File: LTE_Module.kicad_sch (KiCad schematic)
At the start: 57 parts, among them J4 Conn_Coaxial, J8 SIM_Card, Q3 MMBT3904, Q4 BC849, Q5 MMBT3904, Q6 MMBT3904, U10 MIC29302AWD, U6 A7670E, U9 AMS1117-3.3

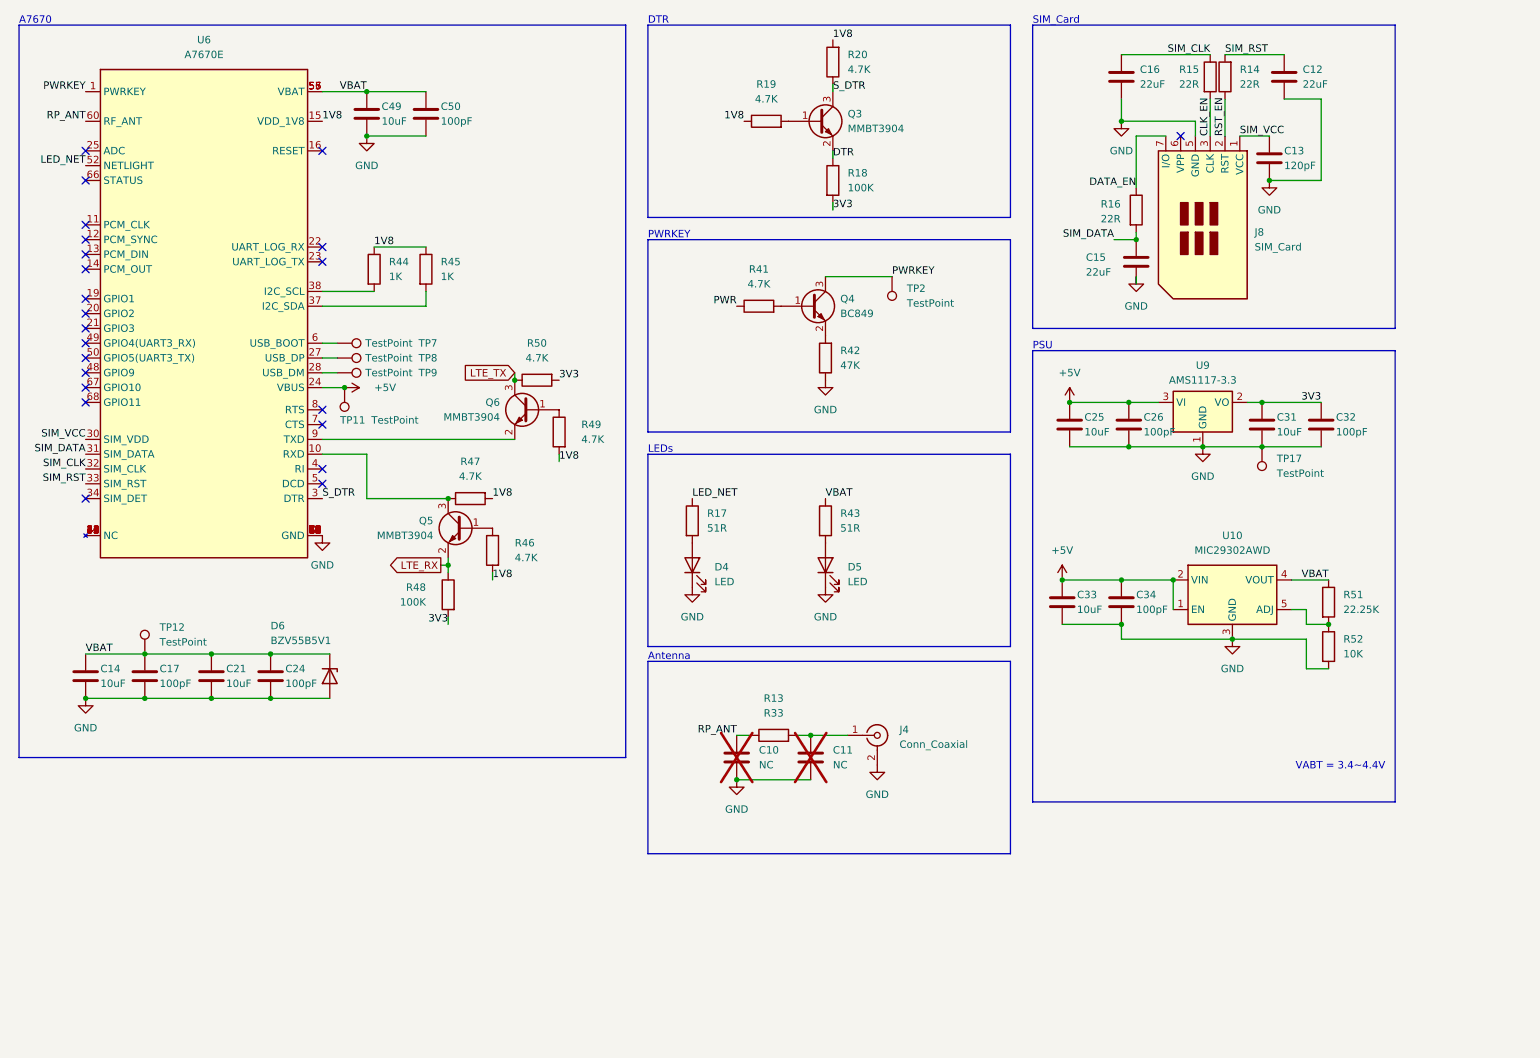
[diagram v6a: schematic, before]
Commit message: assigned most footprints
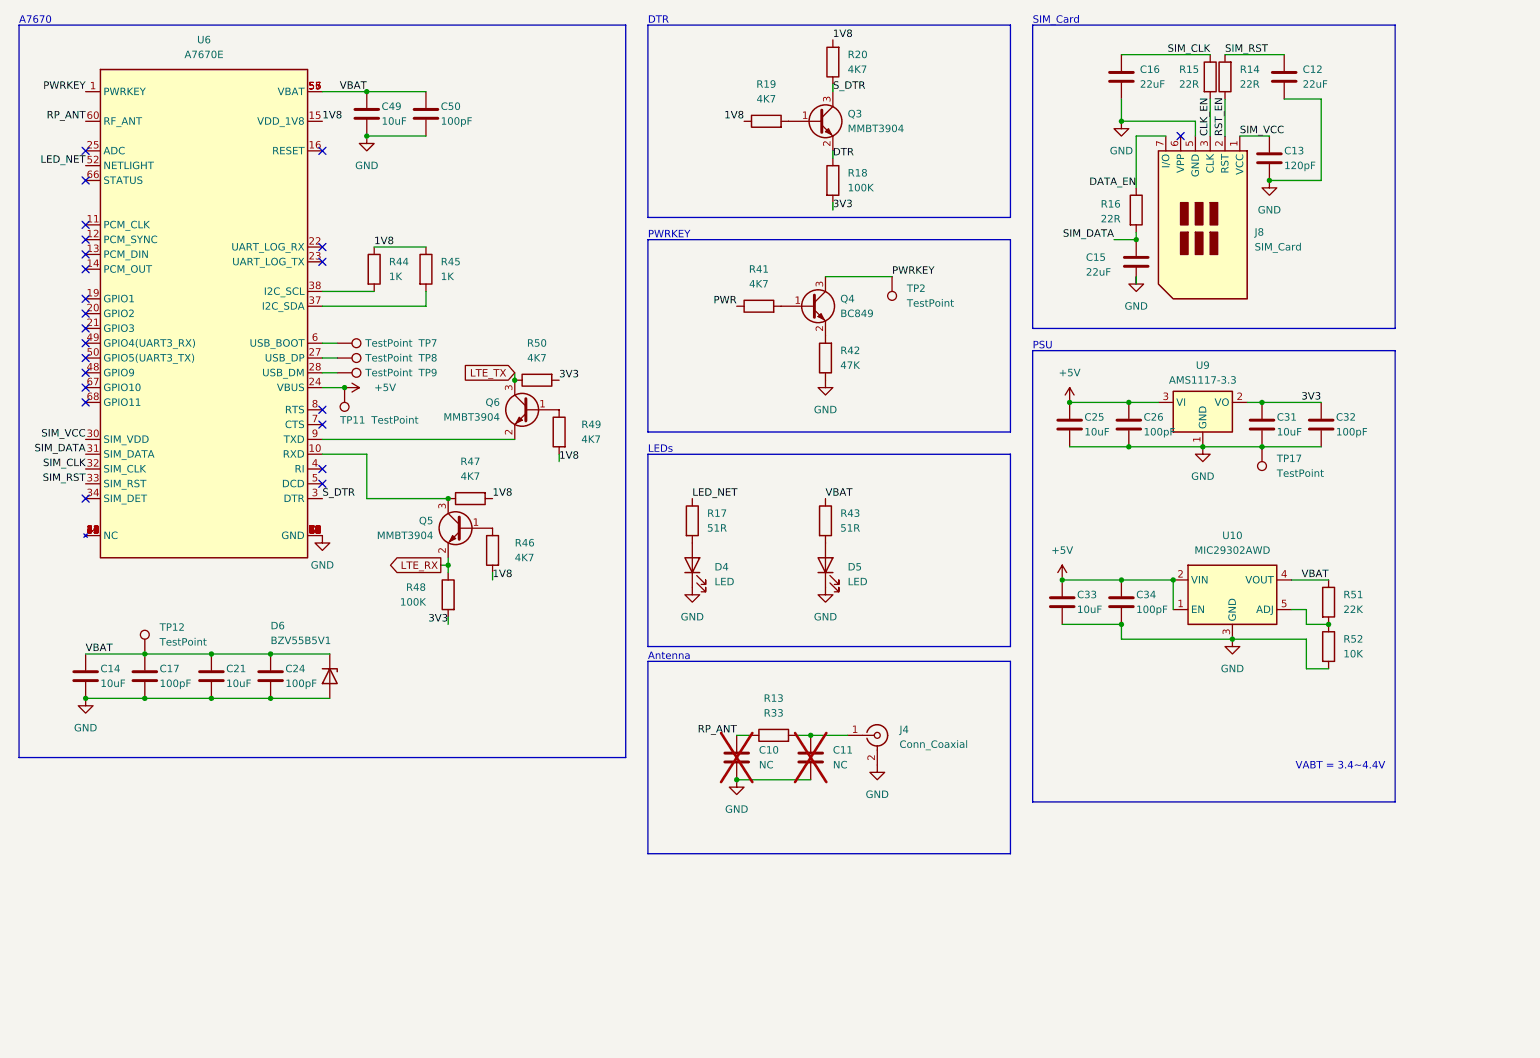
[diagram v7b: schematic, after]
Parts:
- C12, C15, C16: footprint Capacitor_SMD:C_1206_3216Metric_Pad1.33x1.80mm_HandSolder -> (none)
- J8: footprint (none) -> Connector_JAE:JAE_SIM_Card_SF72S006
- R13, R14, R15, R16, R17, R18, R42, R43, R44, R45, R48, R52: footprint (none) -> Resistor_SMD:R_0603_1608Metric
- R19, R20, R41, R46, R47, R49, R50: value 4.7K -> 4K7; footprint (none) -> Resistor_SMD:R_0603_1608Metric
- R51: value 22.25K -> 22K; footprint (none) -> Resistor_SMD:R_0603_1608Metric
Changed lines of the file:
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@@
 			)
 		)
-		(property "Footprint" "Capacitor_SMD:C_1206_3216Metric_Pad1.33x1.80mm_HandSolder"
+		(property "Footprint" ""
 			(at 206.7052 29.21 0)
 			(effects
@@
 			)
 		)
-		(property "Value" "22.25K"
+		(property "Value" "22K"
 			(at 243.84 116.8399 0)
 			(effects
@@
 			)
 		)
-		(property "Footprint" ""
+		(property "Footprint" "Resistor_SMD:R_0603_1608Metric"
 			(at 239.522 115.57 90)
 			(effects
@@
 			)
 		)
-		(property "Value" "4.7K"
+		(property "Value" "4K7"
 			(at 143.51 60.96 90)
 			(effects
@@
 			)
 		)
-		(property "Footprint" ""
+		(property "Footprint" "Resistor_SMD:R_0603_1608Metric"
 			(at 143.51 66.548 90)
 			(effects
@@
 			)
 		)
-		(property "Footprint" "Capacitor_SMD:C_1206_3216Metric_Pad1.33x1.80mm_HandSolder"
+		(property "Footprint" ""
 			(at 234.6452 29.21 0)
 			(effects
@@
 			)
 		)
-		(property "Footprint" ""
+		(property "Footprint" "Resistor_SMD:R_0603_1608Metric"
 			(at 225.298 25.4 90)
 			(effects
@@
 			)
 		)
-		(property "Value" "4.7K"
+		(property "Value" "4K7"
 			(at 101.6 107.9499 0)
 			(effects
@@
 			)
 		)
-		(property "Footprint" ""
+		(property "Footprint" "Resistor_SMD:R_0603_1608Metric"
 			(at 99.568 106.68 90)
 			(effects
@@
 			)
 		)
-		(property "Footprint" ""
+		(property "Footprint" "Resistor_SMD:R_0603_1608Metric"
 			(at 219.202 25.4 90)
 			(effects
@@
 			)
 		)
-		(property "Footprint" ""
+		(property "Footprint" "Resistor_SMD:R_0603_1608Metric"
 			(at 239.522 123.19 90)
 			(effects
@@
 			)
 		)
-		(property "Footprint" ""
+		(property "Footprint" "Resistor_SMD:R_0603_1608Metric"
 			(at 154.432 43.18 90)
 			(effects
@@
 			)
 		)
-		(property "Footprint" ""
+		(property "Footprint" "Connector_JAE:JAE_SIM_Card_SF72S006"
 			(at 227.33 48.26 0)
 			(effects
@@
 			)
 		)
-		(property "Value" "4.7K"
+		(property "Value" "4K7"
 			(at 144.78 29.21 90)
 			(effects
@@
 			)
 		)
-		(property "Footprint" ""
+		(property "Footprint" "Resistor_SMD:R_0603_1608Metric"
 			(at 144.78 34.798 90)
 			(effects
@@
 			)
 		)
-		(property "Footprint" ""
+		(property "Footprint" "Resistor_SMD:R_0603_1608Metric"
 			(at 75.692 58.42 90)
 			(effects
@@
 			)
 		)
-		(property "Value" "4.7K"
+		(property "Value" "4K7"
 			(at 93.98 93.98 90)
 			(effects
@@
 			)
 		)
-		(property "Footprint" ""
+		(property "Footprint" "Resistor_SMD:R_0603_1608Metric"
 			(at 93.98 96.012 90)
 			(effects
@@
 			)
 		)
-		(property "Footprint" "Capacitor_SMD:C_1206_3216Metric_Pad1.33x1.80mm_HandSolder"
+		(property "Footprint" ""
 			(at 209.2452 60.96 0)
 			(effects
@@
 			)
 		)
-		(property "Footprint" ""
+		(property "Footprint" "Resistor_SMD:R_0603_1608Metric"
 			(at 206.502 48.26 90)
 			(effects
@@
 			)
 		)
-		(property "Value" "4.7K"
+		(property "Value" "4K7"
 			(at 113.03 87.6299 0)
 			(effects
@@
 			)
 		)
-		(property "Footprint" ""
+		(property "Footprint" "Resistor_SMD:R_0603_1608Metric"
 			(at 110.998 86.36 90)
 			(effects
@@
 			)
 		)
-		(property "Footprint" ""
+		(property "Footprint" "Resistor_SMD:R_0603_1608Metric"
 			(at 153.162 101.6 90)
 			(effects
@@
 			)
 		)
-		(property "Footprint" ""
+		(property "Footprint" "Resistor_SMD:R_0603_1608Metric"
 			(at 84.582 58.42 90)
 			(effects
@@
 			)
 		)
-		(property "Footprint" ""
+		(property "Footprint" "Resistor_SMD:R_0603_1608Metric"
 			(at 156.718 73.66 90)
 			(effects
@@
 			)
 		)
-		(property "Footprint" ""
+		(property "Footprint" "Resistor_SMD:R_0603_1608Metric"
 			(at 130.302 101.6 90)
 			(effects
@@
 			)
 		)
-		(property "Footprint" ""
+		(property "Footprint" "Resistor_SMD:R_0603_1608Metric"
 			(at 91.948 114.3 90)
 			(effects
@@
 			)
 		)
-		(property "Value" "4.7K"
+		(property "Value" "4K7"
 			(at 105.41 73.66 90)
 			(effects
@@
 			)
 		)
-		(property "Footprint" ""
+		(property "Footprint" "Resistor_SMD:R_0603_1608Metric"
 			(at 105.41 75.692 90)
 			(effects
@@
 			)
 		)
-		(property "Value" "4.7K"
+		(property "Value" "4K7"
 			(at 158.75 24.1299 0)
 			(effects
@@
 			)
 		)
-		(property "Footprint" ""
+		(property "Footprint" "Resistor_SMD:R_0603_1608Metric"
 			(at 157.988 22.86 90)
 			(effects
@@
 			)
 		)
-		(property "Footprint" ""
+		(property "Footprint" "Resistor_SMD:R_0603_1608Metric"
 			(at 146.05 140.208 90)
 			(effects

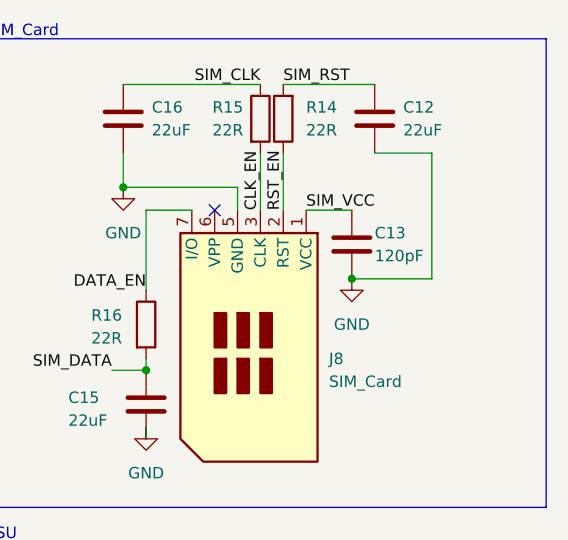
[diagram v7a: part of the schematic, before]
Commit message: cleaned up scematics and updated power management
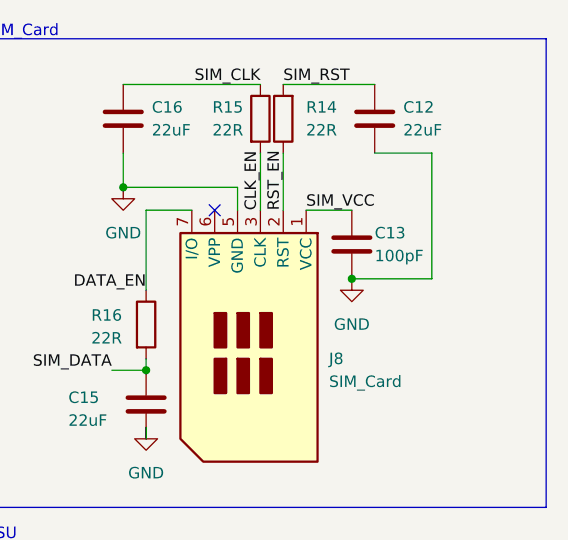
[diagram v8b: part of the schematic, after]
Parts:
- C10, C11, C17, C24, C26, C32, C34, C50: footprint (none) -> Capacitor_SMD:C_0805_2012Metric
- C12, C15, C16: footprint (none) -> Capacitor_SMD:C_0603_1608Metric
- C13: value 120pF -> 100pF; footprint (none) -> Capacitor_SMD:C_0805_2012Metric
- C14, C21, C25, C31, C33, C49: footprint (none) -> Capacitor_SMD:C_1206_3216Metric
